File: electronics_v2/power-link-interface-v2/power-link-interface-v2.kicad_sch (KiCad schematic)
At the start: 39 parts

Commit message: PLI work
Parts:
- removed J?: Conn_01x02, Connector_AMASS:AMASS_XT60-M_1x02_P7.20mm_Vertical, symbol Connector_Generic:Conn_01x02
- removed R? (x5): 10m, Resistor_SMD:R_2512_6332Metric, symbol Device:R
- added J1: Conn_01x02, Connector_AMASS:AMASS_XT60-M_1x02_P7.20mm_Vertical, symbol Connector_Generic:Conn_01x02
- added Q1: IRFR5305, Package_TO_SOT_SMD:TO-252-2, symbol Device:Q_PMOS_GDS
- added R1: 10k, Resistor_SMD:R_0603_1608Metric, symbol Device:R
- added R11, R12, R7, R8, R9: 10m, Resistor_SMD:R_1206_3216Metric, symbol Device:R
- added R2: 1k, Resistor_SMD:R_0603_1608Metric, symbol Device:R
- added SW1: SW_Push_SPDT, goose:tht_pin_01x03, symbol Switch:SW_Push_SPDT
- added U1: ESC, goose:ESC, symbol goose:ESC
- C1: renamed from C?; value 470u/16V -> 470u/25V; footprint (none) -> Capacitor_THT:C_Radial_D8.0mm_H11.5mm_P3.50mm
- D2: renamed from D?; value SS36A -> SS34
- J2: renamed from J?; footprint (none) -> goose:tht_pin_01x03
- J4, J5, J6, J7: renamed from J?; footprint (none) -> Connector_PinHeader_2.54mm:PinHeader_1x03_P2.54mm_Vertical
- L1: renamed from L?; footprint Inductor_SMD:L_12x12mm_H6mm -> Inductor_SMD:L_AVX_LMLP07A7
- R15, R16: renamed from R?; value 4k7 -> 10k
- R17, R18: renamed from R?; value 210k -> 470k
- gave numbers to parts that had none: 20
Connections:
- net +BATT: now also R11.1, R12.1, R7.1, R8.1, R9.1, U1.1 (SUPPLY)
- net GND: now also J1.1 (Pin_1), SW1.1 (A), U1.2 (GND), U1.8 (GND)
- net PWM_ESC: now also U1.6 (SIGNAL)
- net COMP-: now reaches R16.2, R18.1, U3.2 (-)
- net COMP+: now reaches R15.1, R17.2, U3.3 (+)
- net L1: now reaches J2.1 (Pin_1)
- net L1: now also U1.3 (L1)
- net L2: now reaches J2.2 (Pin_2)
- net L2: now also U1.4 (L2)
- net L3: now reaches J2.3 (Pin_3)
- net L3: now also U1.5 (L3)
- net BATT_IN renamed SUPPLY
- net SUPPLY: now also Q1.2 (D), R11.2, R12.2, R7.2, R8.2, R9.2
- new net: R2.2, SW1.2 (B)
- new net BATTERY_IN: J1.2 (Pin_2), Q1.3 (S), R1.1
- new net MOSFET_GATE: Q1.1 (G), R1.2, R2.1
- no-connect marks 2 -> 4
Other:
- note added: "gain = 47"
- note added: "measurement"
- note added: "pomair prądu: - wybrać OpAmpa kątowe wejście XT60"
- note added: "should be 0.8V"
- note added: "supply management"
- note added: "supply voltage"
- note removed: "battery voltage measurement"
- note removed: "current sense gain calculations: for: R31 = R33 R32 = R34 Vout = (R34/R33) * Rshunt*Ibatt R34 = (Vout * R33)/(Rshunt*Ibatt) assume: Ibatt = 70 A Rshunt = 0.001 ohm Vout = 3.1 V R33 = 4.7 kohm then: R34 = (3.1 * 4700)/(0.001*70) = 210 kohm"
- note removed: "shunt resistor power calculations: Pshunt = Rshunt * I^2 assume: Rshunt = 0.001 ohm I = 50 A then: Pshunt = 0.001 * 50^2 = 2.5 W for 2512 resistor: Pmax = 3 W"
- note removed: "symbol + footprint ESC footprinty do przetwornicy opamp rail-to-rail + obliczenia"
- note removed: "voltage divider calcualtions: U_out = U_in * R12/(R11 + R12) U_out * (R11 + R12) = U_in * R12 U_out * R11 + U_out * R12 = U_in * R12 U_out * R11 = R12 * (U_in - U_out) R11 = R12 * (U_in - U_out)/U_out assume: R12 = 100 kohm U_in = 12.4 V U_out = 3.1 V then: R11 = 100k * (12.4-3.1)/3.1 = 300 kohm"
- moved on the sheet: C1, C2, C3, C4, C5, C6, D1, D2, H1, H2, H3, H4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

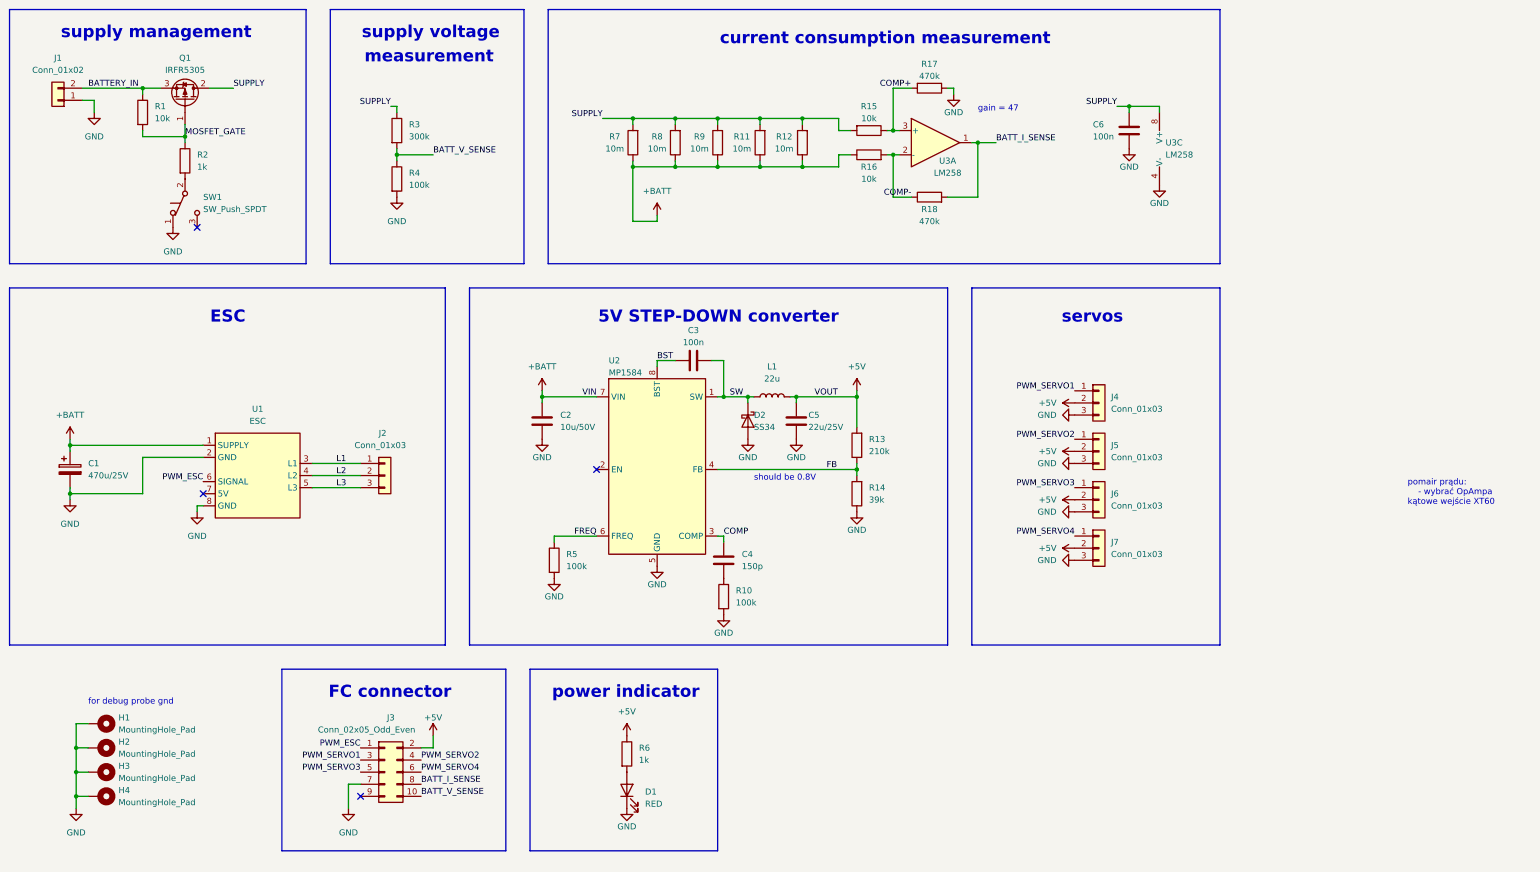
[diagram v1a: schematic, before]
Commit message: edge XT60 connector & INA226 I2C measurement
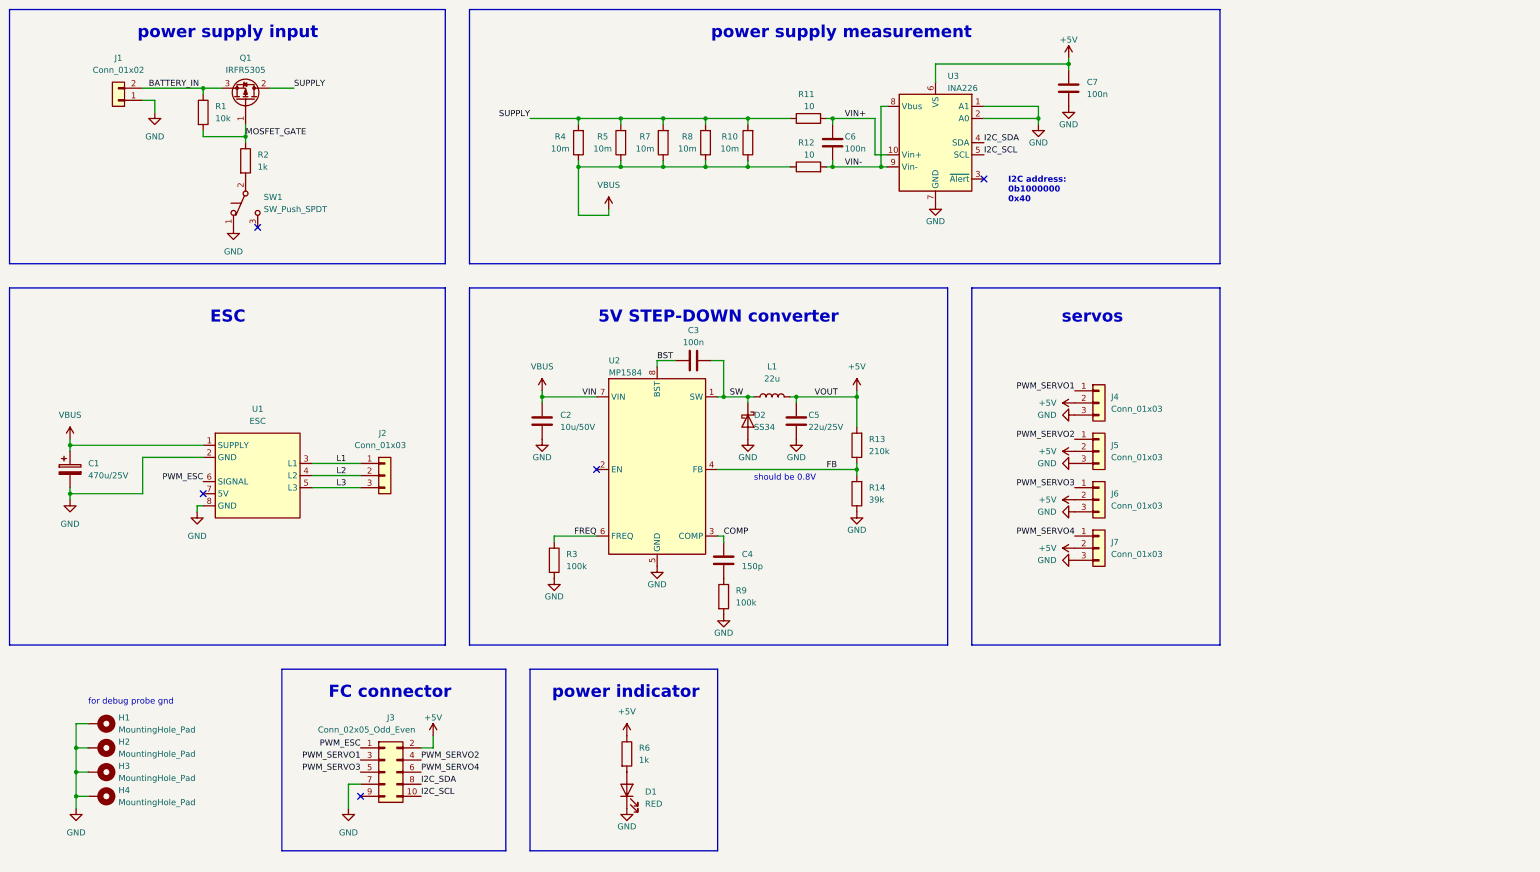
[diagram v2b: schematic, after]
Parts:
- removed R15, R16: 10k, Resistor_SMD:R_0603_1608Metric, symbol Device:R
- removed R17, R18: 470k, Resistor_SMD:R_0603_1608Metric, symbol Device:R
- removed R3: 300k, Resistor_SMD:R_0603_1608Metric, symbol Device:R
- removed R4: 100k, Resistor_SMD:R_0603_1608Metric, symbol Device:R
- removed U3: LM258, Package_SO:SOIC-8_3.9x4.9mm_P1.27mm, symbol Amplifier_Operational:LM358
- added C6: 100n, Capacitor_SMD:C_0603_1608Metric, symbol Device:C
- added R11, R12: 10, Resistor_SMD:R_0603_1608Metric, symbol Device:R
- added U3: INA226, Package_SO:VSSOP-10_3x3mm_P0.5mm, symbol Analog_ADC:INA226
- J1: footprint Connector_AMASS:AMASS_XT60-M_1x02_P7.20mm_Vertical -> goose:AMASS_XT60PW-M
- renumbered C6 to C7, R12 to R10, R5 to R3, R7 to R4, R8 to R5, R9 to R7, R11 to R8, R10 to R9
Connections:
- net +5V: now also C7.2, U3.6 (VS)
- net GND: now also U3.1 (A1), U3.2 (A0), U3.7 (GND)
- net SUPPLY: now also R11.1; no longer C7.2
- net +BATT renamed VBUS
- net VBUS: now also R12.1
- net BATT_I_SENSE renamed I2C_SDA
- net I2C_SDA: now also U3.4 (SDA)
- net BATT_V_SENSE renamed I2C_SCL
- net I2C_SCL: now also U3.5 (SCL)
- new net VIN+: C6.2, R11.2, U3.10 (Vin+)
- new net VIN-: C6.1, R12.2, U3.8 (Vbus), U3.9 (Vin-)
- no-connect marks 4 -> 5
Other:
- note added: "I2C address: 0b1000000 0x40"
- note added: "power supply input"
- note added: "power supply measurement"
- note removed: "current consumption measurement"
- note removed: "gain = 47"
- note removed: "measurement"
- note removed: "pomair prądu: - wybrać OpAmpa kątowe wejście XT60"
- note removed: "supply management"
- note removed: "supply voltage"
- moved on the sheet: C7, J1, Q1, R1, R10, R2, R4, R5, R7, R8, SW1

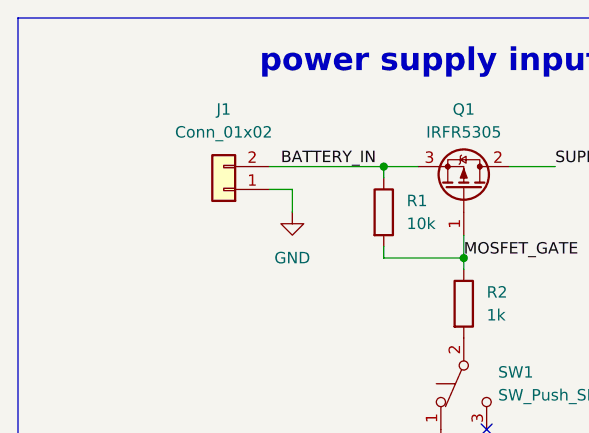
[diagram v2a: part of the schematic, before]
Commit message: move XT60 to center of the edge
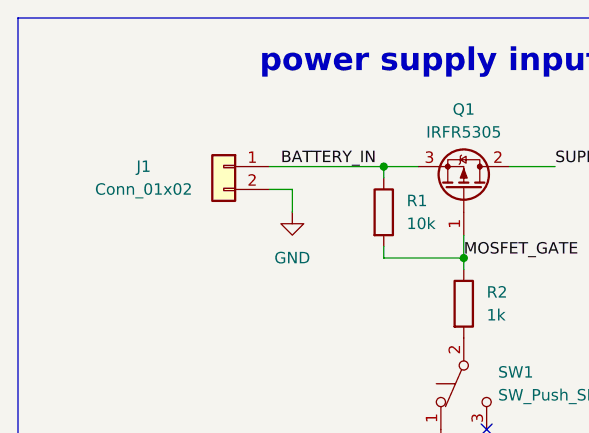
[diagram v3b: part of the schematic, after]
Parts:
- SW1: footprint goose:tht_pin_01x03 -> Button_Switch_THT:SW_CuK_JS202011CQN_DPDT_Straight
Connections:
- net BATTERY_IN: now also J1.1 (Pin_1); no longer J1.2 (Pin_2)
- net GND: now also J1.2 (Pin_2); no longer J1.1 (Pin_1)
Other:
- moved on the sheet: J1
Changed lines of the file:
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@@
   (junction (at 31.75 171.45) (diameter 0) (color 0 0 0 0)
   )
+  (junction (at 58.42 33.02) (diameter 0) (color 0 0 0 0)
+  )
   (junction (at 163.83 49.53) (diameter 0) (color 0 0 0 0)
   )
@@
   )
   (junction (at 195.58 97.79) (diameter 0) (color 0 0 0 0)
-  )
-  (junction (at 58.42 33.02) (diameter 0) (color 0 0 0 0)
   )
   (junction (at 167.64 97.79) (diameter 0) (color 0 0 0 0)
@@
     (stroke (width 0) (type default) (color 0 0 0 0))
   )
+  (wire (pts (xy 45.72 35.56) (xy 48.26 35.56))
+    (stroke (width 0) (type default) (color 0 0 0 0))
+  )
   (polyline (pts (xy 17.78 74.93) (xy 17.78 149.86))
     (stroke (width 0) (type default) (color 0 0 0 0))
@@
     (stroke (width 0) (type default) (color 0 0 0 0))
   )
+  (wire (pts (xy 45.72 33.02) (xy 58.42 33.02))
+    (stroke (width 0) (type default) (color 0 0 0 0))
+  )
   (wire (pts (xy 200.66 49.53) (xy 201.93 49.53))
     (stroke (width 0) (type default) (color 0 0 0 0))
@@
     (stroke (width 0) (type default) (color 0 0 0 0))
   )
-  (wire (pts (xy 45.72 33.02) (xy 58.42 33.02))
-    (stroke (width 0) (type default) (color 0 0 0 0))
-  )
   (polyline (pts (xy 74.93 193.04) (xy 121.92 193.04))
     (stroke (width 0) (type default) (color 0 0 0 0))
@@
   )
   (polyline (pts (xy 109.22 149.86) (xy 109.22 74.93))
-    (stroke (width 0) (type default) (color 0 0 0 0))
-  )
-  (wire (pts (xy 45.72 35.56) (xy 48.26 35.56))
     (stroke (width 0) (type default) (color 0 0 0 0))
   )
@@
       (effects (font (size 1.27 1.27)) (justify right))
     )
-    (property "Footprint" "goose:tht_pin_01x03" (id 2) (at 67.31 57.15 0)
+    (property "Footprint" "Button_Switch_THT:SW_CuK_JS202011CQN_DPDT_Straight" (id 2) (at 67.31 57.15 0)
       (effects (font (size 1.27 1.27)) hide)
     )
@@
     (pin "1")
   )
-  (symbol (lib_id "Connector_Generic:Conn_01x02") (at 40.64 35.56 180) (unit 1)
-    (in_bom yes) (on_board yes)
-    (property "Reference" "J1" (id 0) (at 40.64 26.67 0))
-    (property "Value" "Conn_01x02" (id 1) (at 40.64 29.21 0))
-    (property "Footprint" "goose:AMASS_XT60PW-M" (id 2) (at 40.64 35.56 0)
-      (effects (font (size 1.27 1.27)) hide)
-    )
-    (property "Datasheet" "~" (id 3) (at 40.64 35.56 0)
+  (symbol (lib_id "Connector_Generic:Conn_01x02") (at 40.64 33.02 0) (mirror y) (unit 1)
+    (in_bom yes) (on_board yes)
+    (property "Reference" "J1" (id 0) (at 31.75 33.02 0))
+    (property "Value" "Conn_01x02" (id 1) (at 31.75 35.56 0))
+    (property "Footprint" "goose:AMASS_XT60PW-M" (id 2) (at 40.64 33.02 0)
+      (effects (font (size 1.27 1.27)) hide)
+    )
+    (property "Datasheet" "~" (id 3) (at 40.64 33.02 0)
       (effects (font (size 1.27 1.27)) hide)
     )
@@
     )
     (path "/455267e4-2137-44ad-b523-799346ecbd04"
-      (reference "SW1") (unit 1) (value "SW_Push_SPDT") (footprint "goose:tht_pin_01x03")
+      (reference "SW1") (unit 1) (value "SW_Push_SPDT") (footprint "Button_Switch_THT:SW_CuK_JS202011CQN_DPDT_Straight")
     )
     (path "/a898591c-0768-437a-997a-4f61aa90fa27"
